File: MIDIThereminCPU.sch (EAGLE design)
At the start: 55 parts, among them IC1 UA78M05DCY, IC2 74AHC1G04DCK, IC3 74AHC1G04DCK, J1 DCJ0202, Q1 16MHz, U1 ATMEGA328P-AU

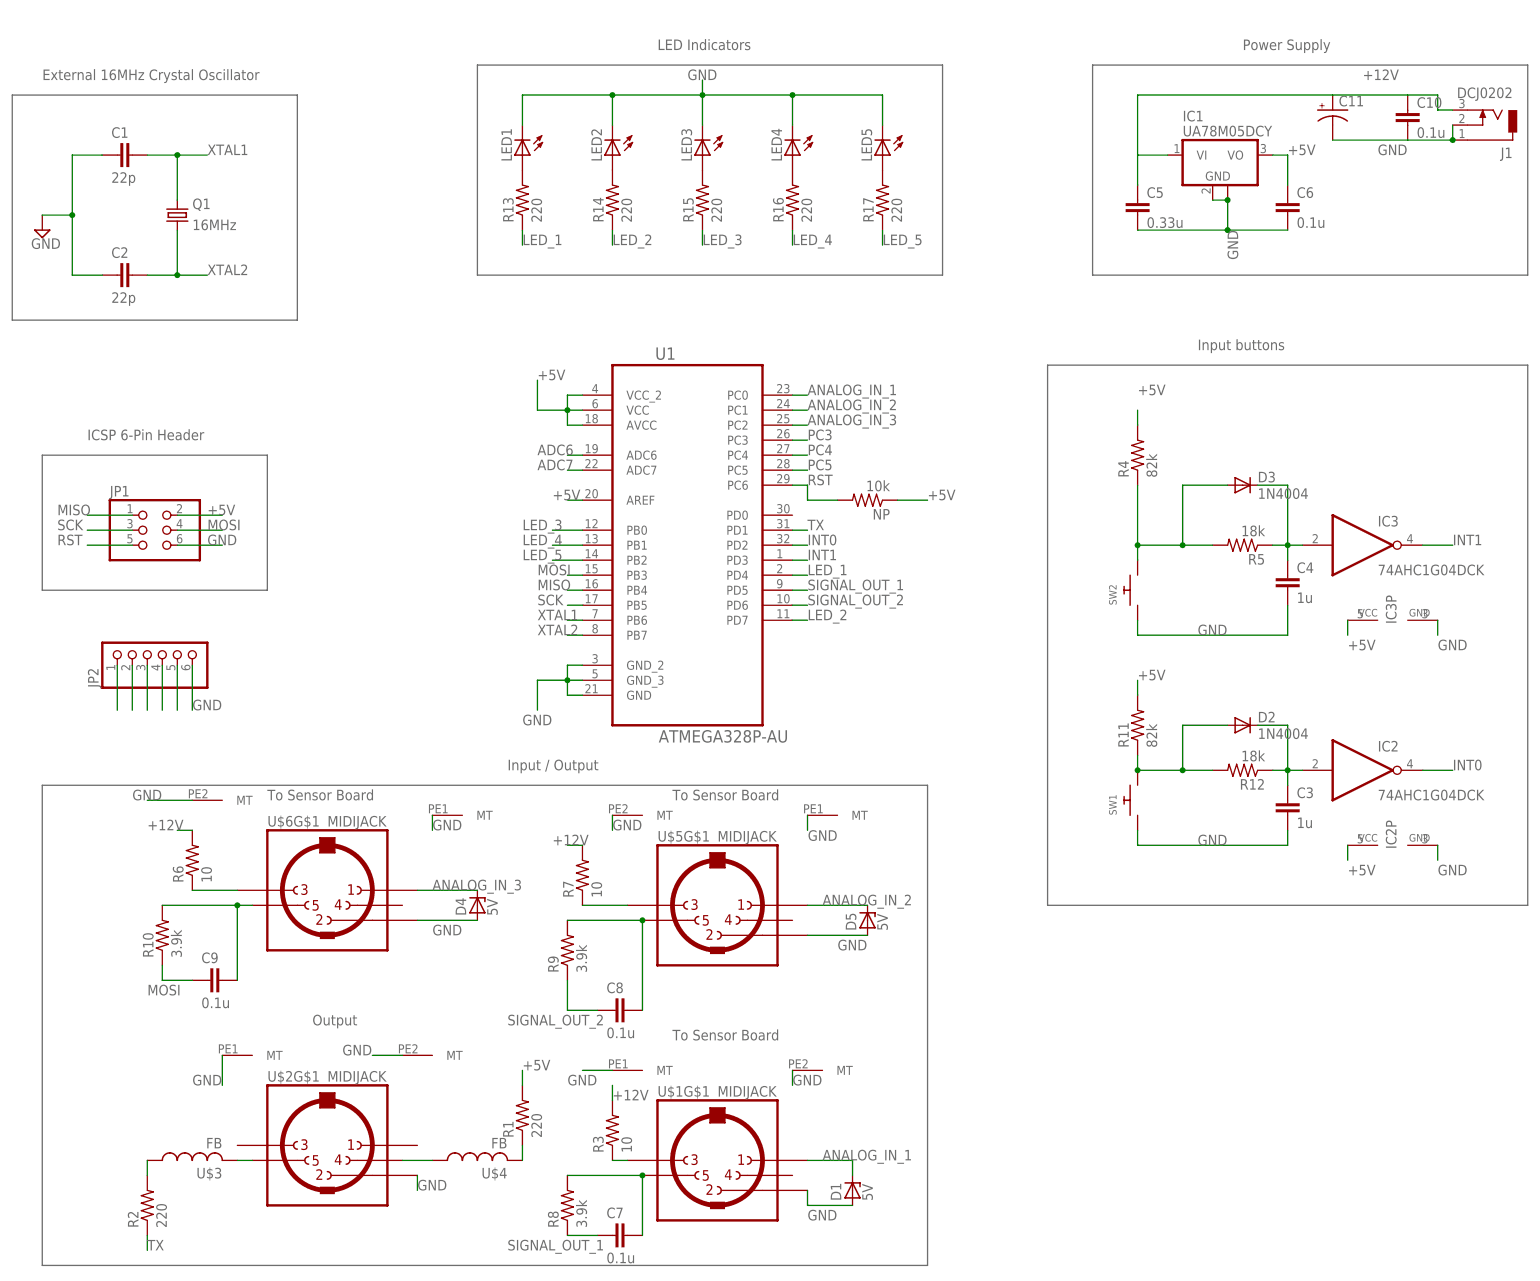
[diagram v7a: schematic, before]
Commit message: changes per discussion
added test points and unused pin headers. pull up resistor on reset. are +5V. barrel jack wired correctly.
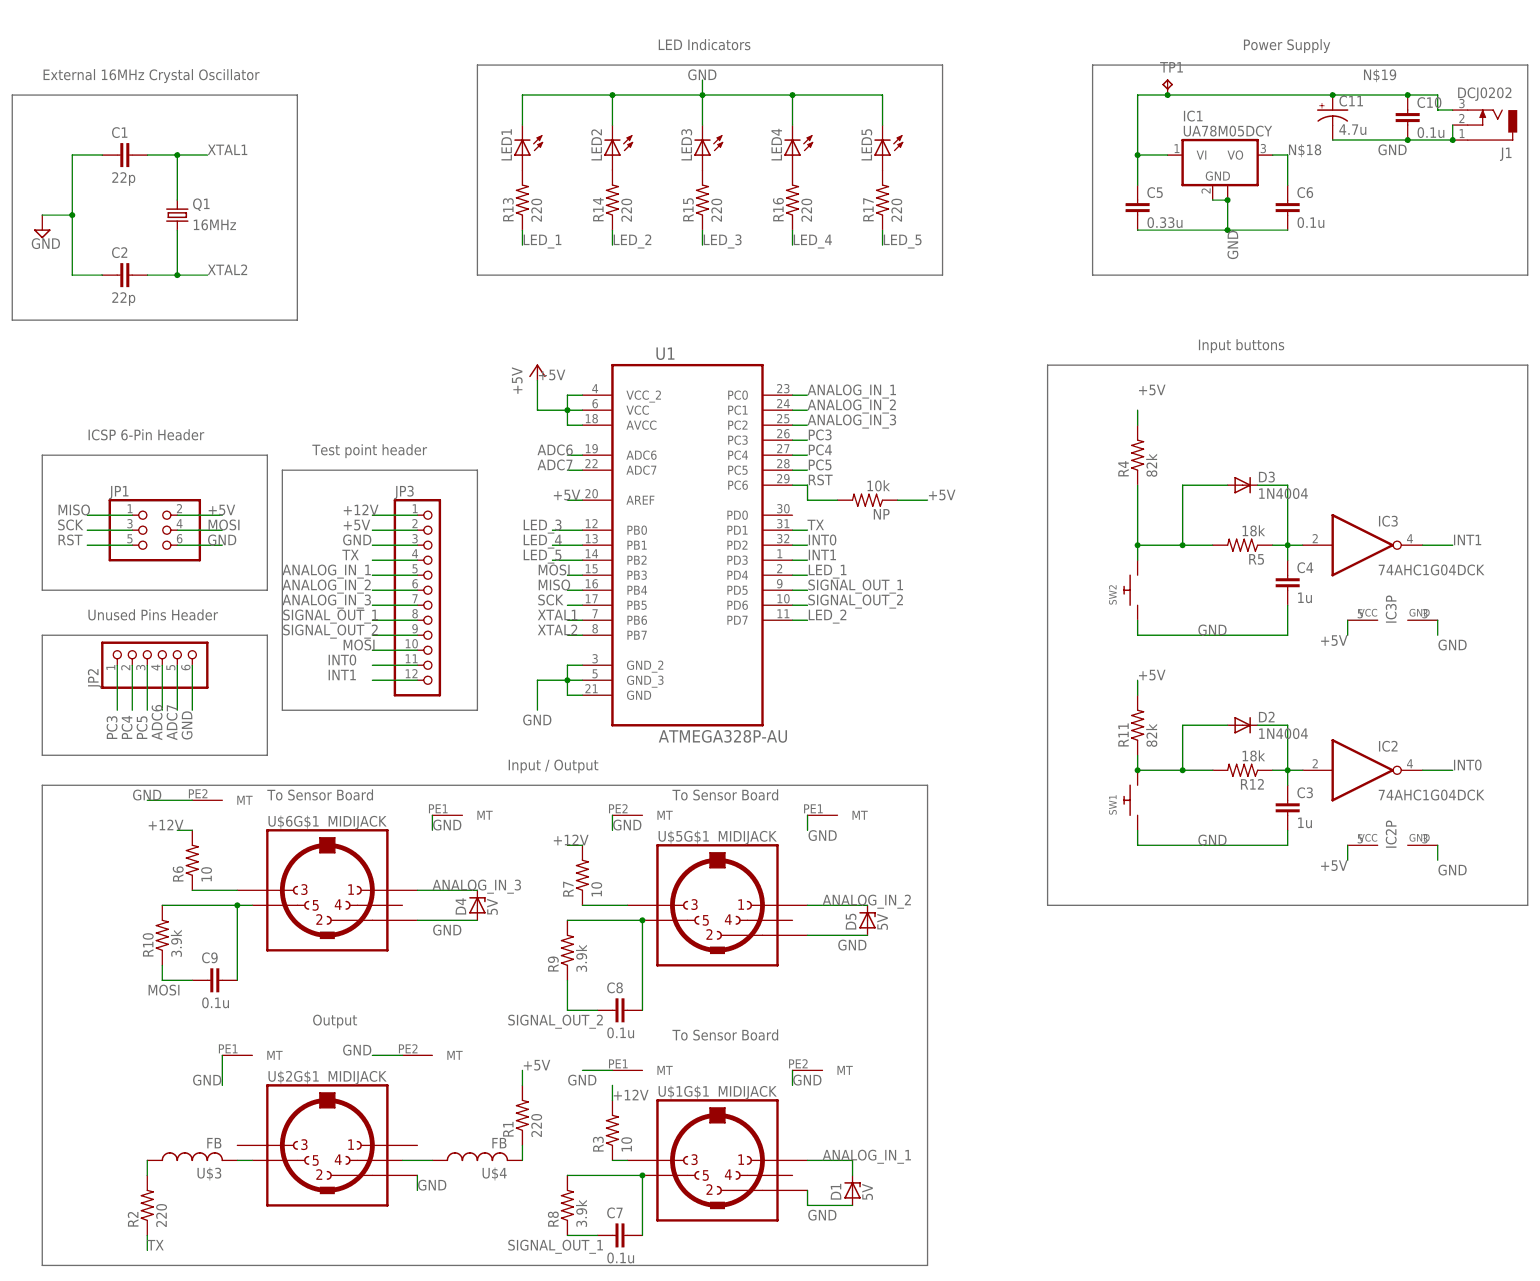
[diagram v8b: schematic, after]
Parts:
- added JP3: (no value), adafruit:PINHD-1X12
- added TP1: TPTP15SQ, testpad:TPTP15SQ
- C11: value (none) -> 4.7u
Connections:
- removed net N$21: JP2.3
- removed net N$22: JP2.4
- removed net N$23: JP2.5
- net +12V: now also JP3.1; no longer C10.1, C11.+, C5.1, IC1.VI, J1.3
- net +5V: now also JP3.2; no longer C6.1, IC1.VO
- net ADC6: now also JP2.4
- net ADC7: now also JP2.5
- net ANALOG_IN_1: now also JP3.5
- net ANALOG_IN_2: now also JP3.6
- net ANALOG_IN_3: now also JP3.7
- net GND: now also JP3.3
- net INT0: now also JP3.11
- net INT1: now also JP3.12
- net MOSI: now also JP3.10
- net N$18: now also C6.1, IC1.VO; no longer JP2.1
- net N$19: now also C10.1, C11.+, C5.1, IC1.VI, J1.3, TP1.TP; no longer JP2.2
- net PC3: now also JP2.1
- net PC4: now also JP2.2
- net PC5: now also JP2.3
- net SIGNAL_OUT_1: now also JP3.8
- net SIGNAL_OUT_2: now also JP3.9
- net TX: now also JP3.4
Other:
- note added: "Test point header"
- note added: "Unused Pins Header"
